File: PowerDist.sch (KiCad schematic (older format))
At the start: 13 parts, among them J3 PowerConn, U5 RI3-1205S, U6 NCP1117-3.3_SOT223

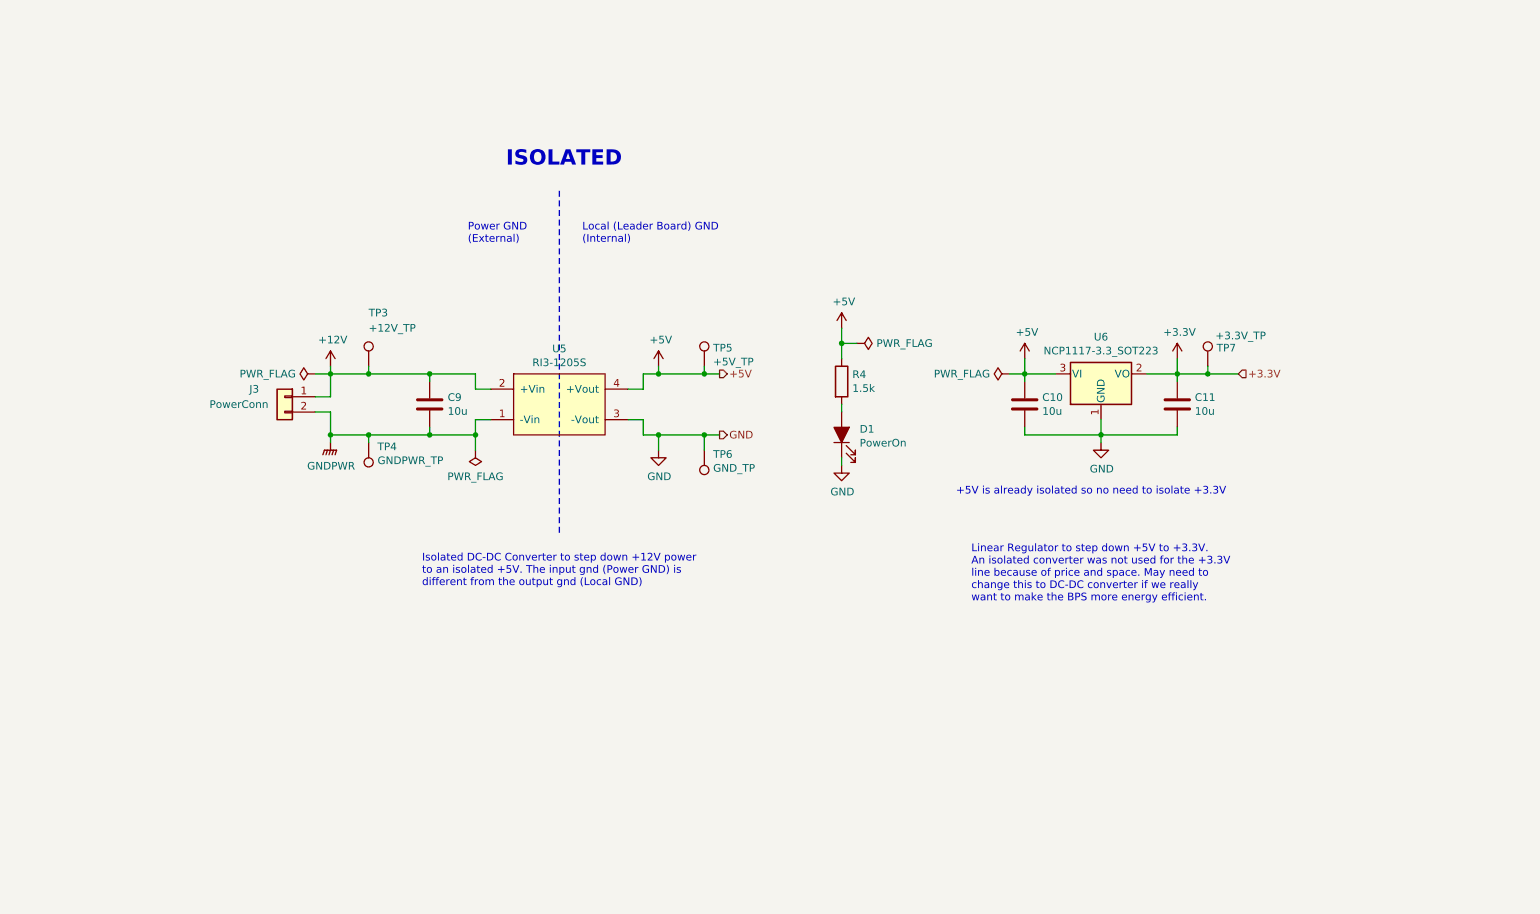
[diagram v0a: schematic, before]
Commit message: Lays out schematic and PCB of v1.0
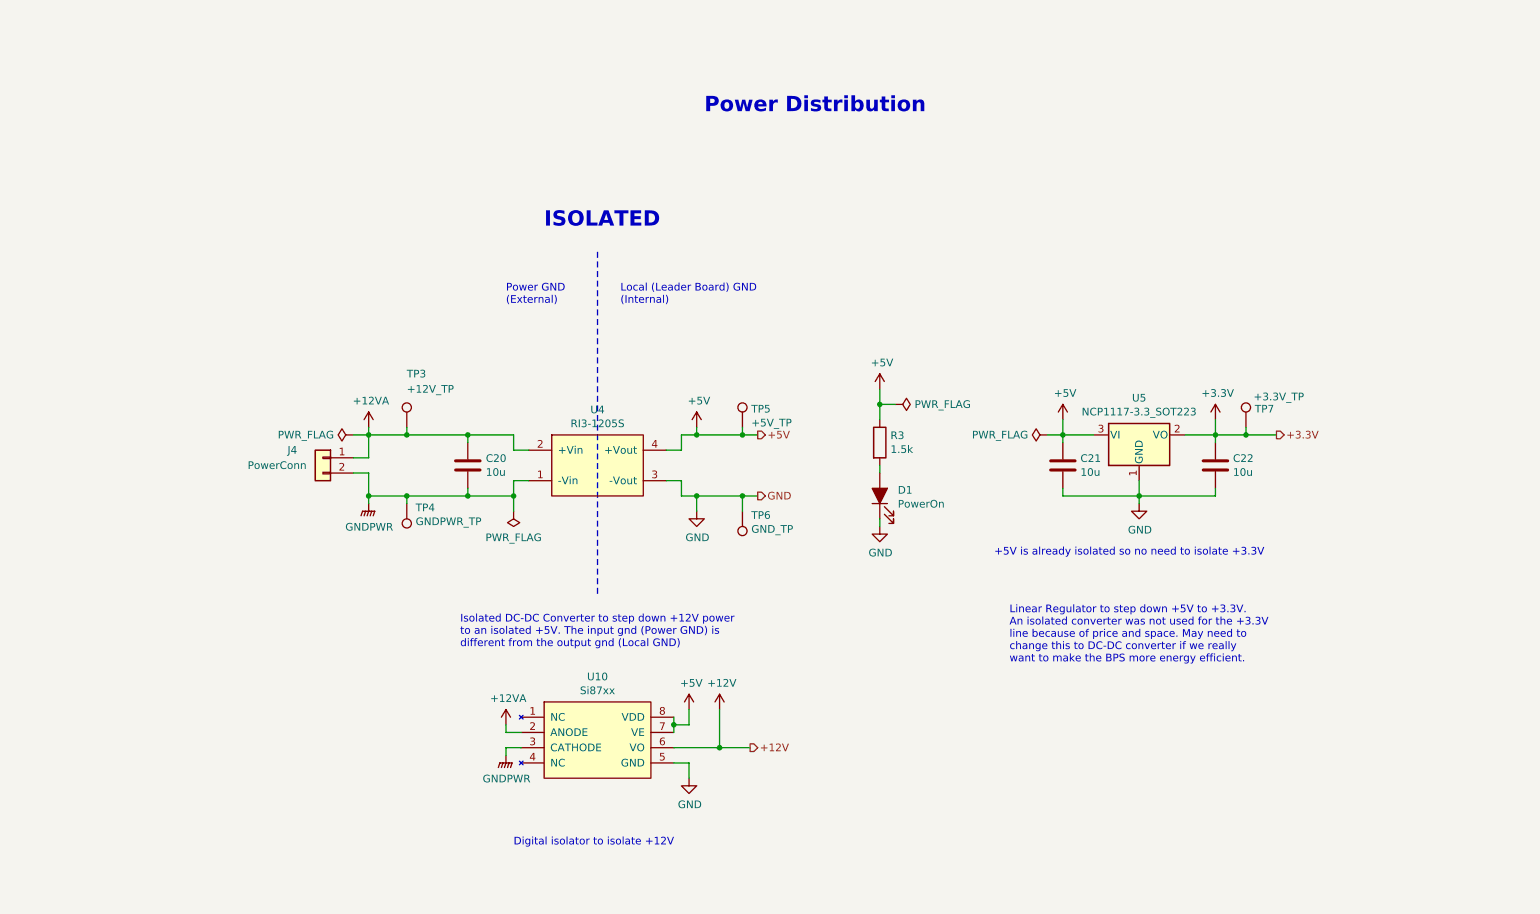
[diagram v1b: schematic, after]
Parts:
- added U10: Si87xx, Package_SO:SOIC-8_3.9x4.9mm_P1.27mm, symbol utsvt-chips:Si87xx
- renumbered C9 to C20, C10 to C21, C11 to C22, J3 to J4, R4 to R3, U5 to U4, U6 to U5
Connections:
- net +12V: now also U10.6 (VO); no longer C20.1, J4.1 (Pin_1), TP3.1, U4.2 (+Vin)
- net +5V: now also U10.7 (VE), U10.8 (VDD)
- net GND: now also U10.5 (GND)
- net GNDPWR: now also U10.3 (CATHODE)
- new net +12VA: C20.1, J4.1 (Pin_1), TP3.1, U10.2 (ANODE), U4.2 (+Vin)
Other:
- note added: "Digital isolator to isolate +12V"
- note added: "Power Distribution"
- moved on the sheet: C20, C21, C22, D1, J4, R3, TP3, TP4, TP5, TP6, TP7, U4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

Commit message: Makes edits from critical design review
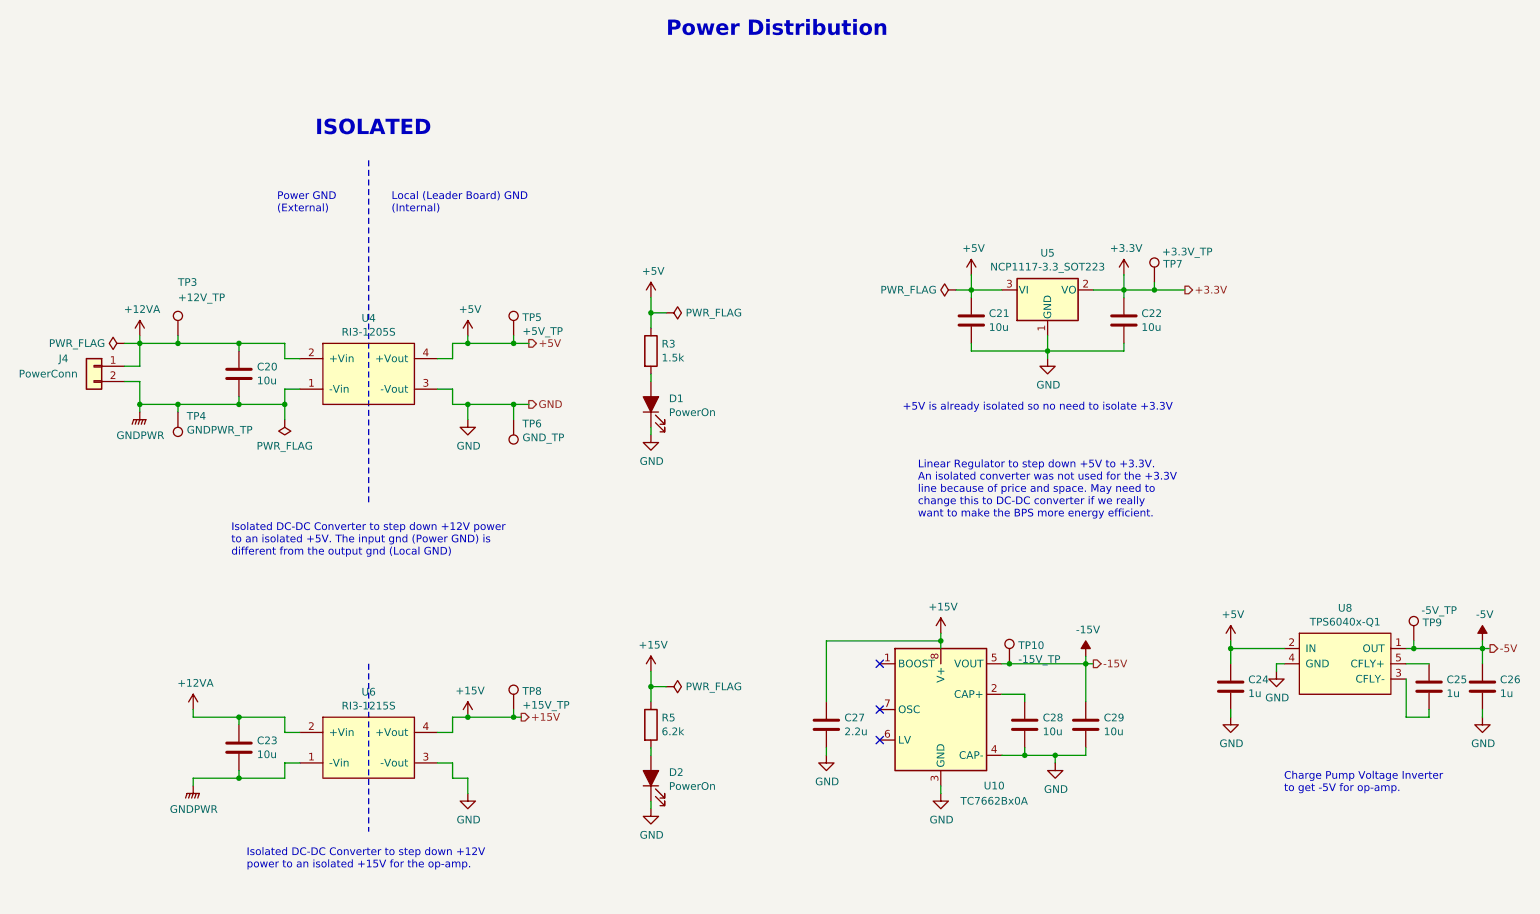
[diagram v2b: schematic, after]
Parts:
- removed U10: Si87xx, Package_SO:SOIC-8_3.9x4.9mm_P1.27mm, symbol utsvt-chips:Si87xx
- added C23: 10u, UTSVT_Passive:C_2220_5750Metric, symbol Device:C
- added C24, C25, C26: 1u, Capacitor_SMD:C_0805_2012Metric, symbol Device:C
- added C27: 2.2u, Capacitor_SMD:C_0805_2012Metric, symbol Device:C
- added C28, C29: 10u, Capacitor_SMD:C_0805_2012Metric, symbol Device:C
- added D2: PowerOn, LED_SMD:LED_0805_2012Metric, symbol Device:LED_ALT
- added R5: 6.2k, Resistor_SMD:R_0805_2012Metric, symbol Device:R
- added TP10: -15V_TP, TestPoint:TestPoint_Keystone_5005-5009_Compact, symbol Connector:TestPoint
- added TP8: +15V_TP, TestPoint:TestPoint_Keystone_5005-5009_Compact, symbol Connector:TestPoint
- added TP9: -5V_TP, TestPoint:TestPoint_Keystone_5005-5009_Compact, symbol Connector:TestPoint
- added U10: TC7662Bx0A, Package_SO:SOIC-8_3.9x4.9mm_P1.27mm, symbol Converter_DCDC:TC7662Bx0A
- added U6: RI3-1215S, UTSVT_ICs:RI3_DC_Converter, symbol utsvt-power-regulators:RI3-1215S
- added U8: TPS6040x-Q1, Package_TO_SOT_SMD:SOT-23-5, symbol utsvt-power-regulators:TPS6040x-Q1
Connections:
- net +12VA: now also C23.1, U6.2 (+Vin)
- net +5V: now also C24.2, U8.2 (IN)
- net GND: now also C24.1, C26.1, C27.2, C28.2, C29.2, D2.1 (K), U10.3 (GND), U10.4 (CAP-), U6.3 (-Vout), U8.4 (GND)
- net GNDPWR: now also C23.2, U6.1 (-Vin)
- new net: D2.2 (A), R5.2
- new net: C25.1, U8.3 (CFLY-)
- new net: C25.2, U8.5 (CFLY+)
- new net: C28.1, U10.2 (CAP+)
- new net +15V: C27.1, R5.1, TP8.1, U10.8 (V+), U6.4 (+Vout)
- new net -15V: C29.1, TP10.1, U10.5 (VOUT)
- new net -5V: C26.2, TP9.1, U8.1 (OUT)
- no-connect marks 0 -> 3
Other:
- note added: "Charge Pump Voltage Inverter \nto get -5V for op-amp."
- note added: "Isolated DC-DC Converter to step down +12V \npower to an isolated +15V for the op-amp."
- note removed: "Digital isolator to isolate +12V"
- moved on the sheet: C20, C21, C22, D1, J4, R3, TP3, TP4, TP5, TP6, TP7, U4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

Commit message: Edits opamp circuitry to just one opamp and adds keepout zone under 12V and GNDPWR
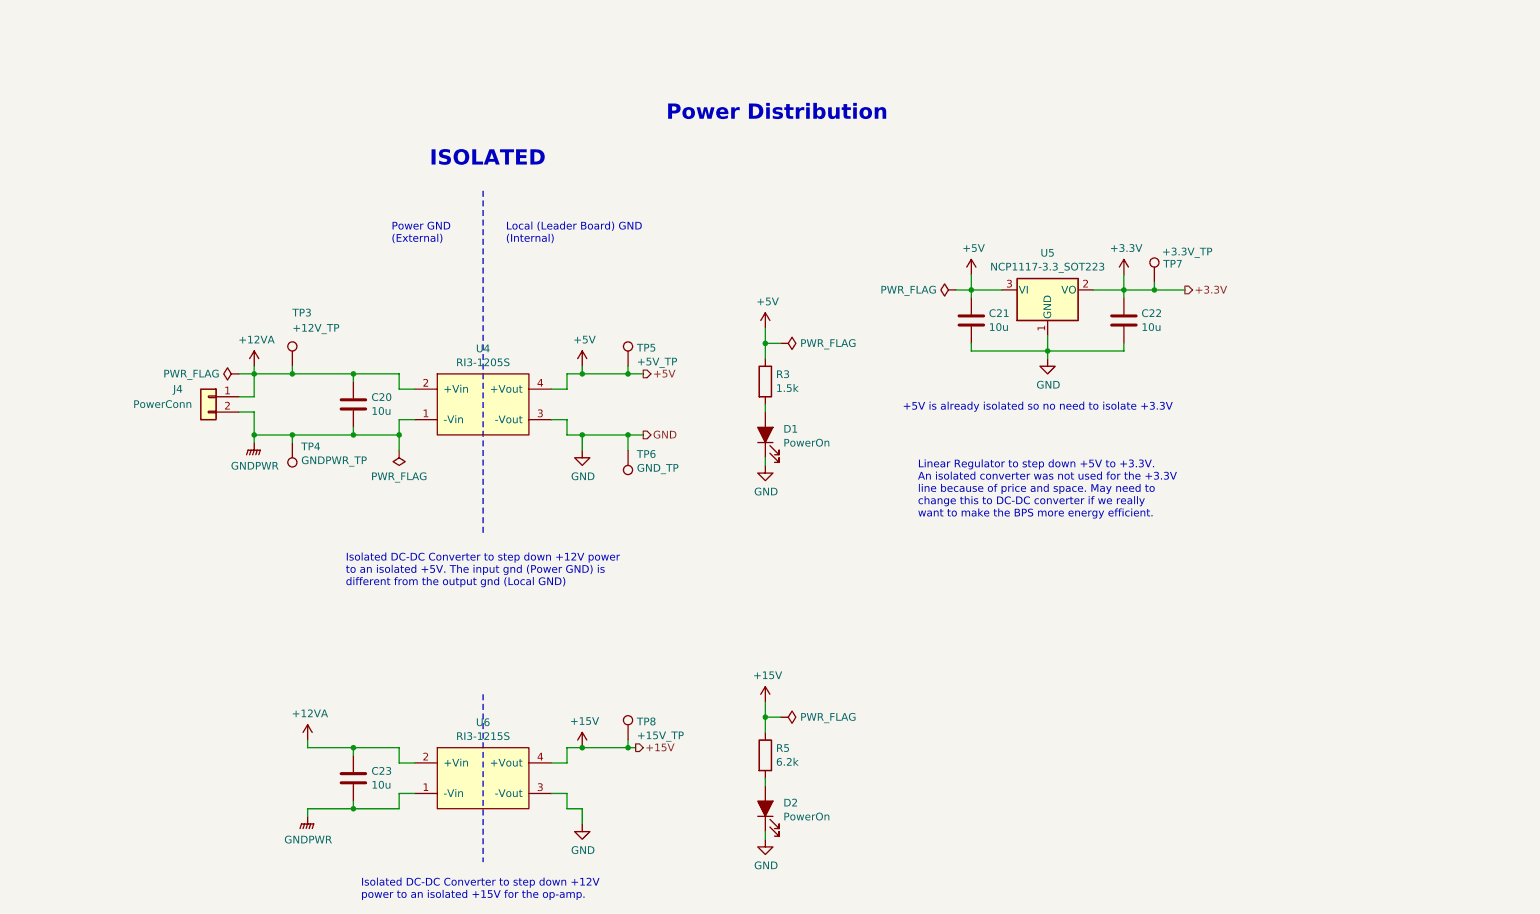
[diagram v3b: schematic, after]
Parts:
- removed C24, C25, C26: 1u, Capacitor_SMD:C_0805_2012Metric, symbol Device:C
- removed C27: 2.2u, Capacitor_SMD:C_0805_2012Metric, symbol Device:C
- removed C28, C29: 10u, Capacitor_SMD:C_0805_2012Metric, symbol Device:C
- removed TP10: -15V_TP, TestPoint:TestPoint_Keystone_5005-5009_Compact, symbol Connector:TestPoint
- removed TP9: -5V_TP, TestPoint:TestPoint_Keystone_5005-5009_Compact, symbol Connector:TestPoint
- removed U10: TC7662Bx0A, Package_SO:SOIC-8_3.9x4.9mm_P1.27mm, symbol Converter_DCDC:TC7662Bx0A
- removed U8: TPS6040x-Q1, Package_TO_SOT_SMD:SOT-23-5, symbol utsvt-power-regulators:TPS6040x-Q1
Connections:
- no-connect marks 3 -> 0
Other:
- note removed: "Charge Pump Voltage Inverter \nto get -5V for op-amp."
- moved on the sheet: C20, C23, D1, D2, J4, R3, R5, TP3, TP4, TP5, TP6, TP8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

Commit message: Correct op amp voltage measurement circuitry
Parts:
- U6: symbol utsvt-power-regulators:RI3-1215S -> Power-SupplementalMonitoringPCB-rescue:RI3-1215S-utsvt-power-regulators
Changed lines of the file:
@@
 Isolated DC-DC Converter to step down +12V \npower to an isolated +15V for the op-amp.
 $Comp
-L utsvt-power-regulators:RI3-1215S U6
+L Power-SupplementalMonitoringPCB-rescue:RI3-1215S-utsvt-power-regulators U6
 U 1 1 5FD5BBD9
 P 4000 5600

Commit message: Fixes opamp circuitry
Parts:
- U6: symbol Power-SupplementalMonitoringPCB-rescue:RI3-1215S-utsvt-power-regulators -> utsvt-power-regulators:RI3-1215S
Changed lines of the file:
@@
 Isolated DC-DC Converter to step down +12V \npower to an isolated +15V for the op-amp.
 $Comp
-L Power-SupplementalMonitoringPCB-rescue:RI3-1215S-utsvt-power-regulators U6
+L utsvt-power-regulators:RI3-1215S U6
 U 1 1 5FD5BBD9
 P 4000 5600
